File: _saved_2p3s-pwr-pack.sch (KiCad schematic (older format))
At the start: 23 parts, among them P1 PAD, P10 PAD, P11 PAD, P12 PAD, P13 Conn_Basic_2_pin, P14 PAD, P15 PAD, P16 Conn_Basic_2_pin, P2 PAD, P3 PAD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

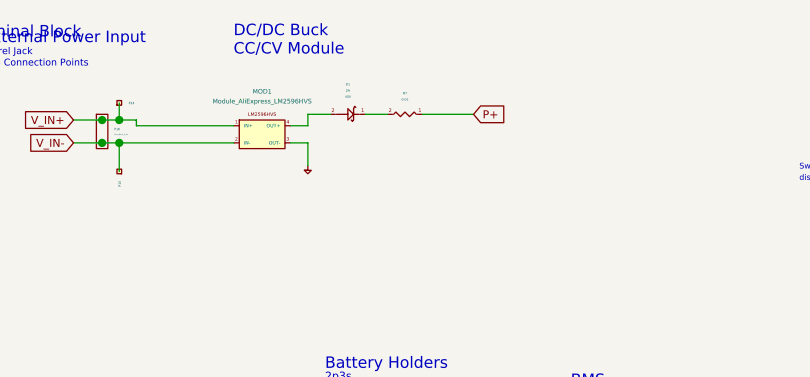
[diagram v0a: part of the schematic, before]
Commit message: Finish JIRA EL-169 changes
move battery holders, change some holes, add current sensing diode, updates to logo, VIN terminal block
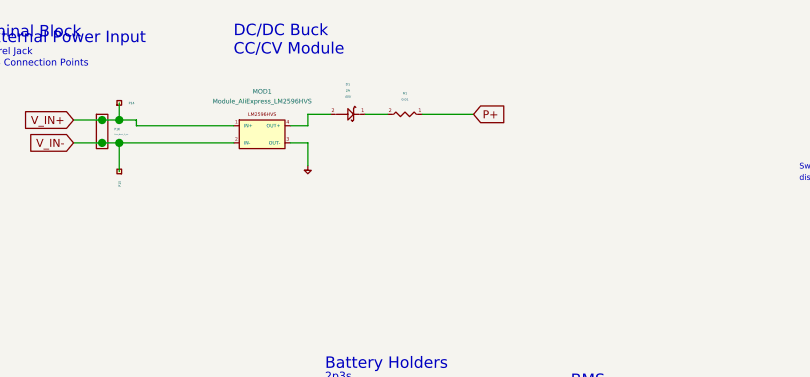
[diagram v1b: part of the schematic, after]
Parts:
- gave numbers to parts that had none: 1
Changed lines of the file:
@@
 Connection ~ 1625 3350
 $Comp
-L __SimpleParts:Res R?
+L __SimpleParts:Res R1
 U 1 1 5CC0A910
 P 2950 3225
-F 0 "R?" V 2858 3225 10  0000 C CNN
+F 0 "R1" V 2858 3225 10  0000 C CNN
 F 1 "0.01" V 2885 3225 10  0000 C CNN
 F 2 "Footprints:1206_Medium_Pads" H 2950 3125 60  0001 C CNN
